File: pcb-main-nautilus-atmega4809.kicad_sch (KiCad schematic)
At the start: 0 parts

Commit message: Add power sheet
Supports #2.
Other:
- added sheet Power (pcb-main-nautilus-atmega4809-sheet-power.kicad_sch)
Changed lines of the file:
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@@
     (comment 1 "Derivative of the \"Arduino UNO Rev3\" (https://docs.arduino.cc/hardware/uno-rev3) and\\n\"Arduino Nano Every\" (https://docs.arduino.cc/hardware/nano-every) reference designs")
+  )
+  (sheet (at 69.85 66.04) (size 19.05 12.7) (fields_autoplaced)
+    (stroke (width 0.1524) (type solid) (color 0 0 0 0))
+    (fill (color 0 0 0 0.0000))
+    (property "Sheet name" "Power" (id 0) (at 69.85 65.3284 0)
+      (effects (font (size 1.27 1.27)) (justify left bottom))
+    )
+    (property "Sheet file" "pcb-main-nautilus-atmega4809-sheet-power.kicad_sch" (id 1) (at 69.85 79.3246 0)
+      (effects (font (size 1.27 1.27)) (justify left top))
+    )
+    (pin "5V" output (at 88.9 71.12 0)
+      (effects (font (size 1.27 1.27)) (justify right))
+    )
+    (pin "USB_VBUS" input (at 69.85 73.66 180)
+      (effects (font (size 1.27 1.27)) (justify left))
+    )
+    (pin "PWRIN" input (at 69.85 68.58 180)
+      (effects (font (size 1.27 1.27)) (justify left))
+    )
+    (pin "VIN" bidirectional (at 69.85 71.12 180)
+      (effects (font (size 1.27 1.27)) (justify left))
+    )
+    (pin "GND" input (at 69.85 76.2 180)
+      (effects (font (size 1.27 1.27)) (justify left))
+    )
+    (pin "3.3V" output (at 88.9 73.66 0)
+      (effects (font (size 1.27 1.27)) (justify right))
+    )
   )
   (sheet_instances
     (path "/" (page "1"))
+    (path "/5a33ba3c-72f7-420a-981d-98ac038c5559" (page "2"))
+  )
+  (symbol_instances
+    (path "/5a33ba3c-72f7-420a-981d-98ac038c5559/7408636a-a4a9-4362-ba4c-0a06147634bc"
+      (reference "C1") (unit 1) (value "47uF/25V") (footprint "")
+    )
+    (path "/5a33ba3c-72f7-420a-981d-98ac038c5559/b6fd6716-59a0-4f9a-985b-c7a8000096b3"
+      (reference "C2") (unit 1) (value "0.1uF/25V") (footprint "Capacitor_SMD:C_0603_1608Metric_Pad1.08x0.95mm_HandSolder")
+    )
+    (path "/5a33ba3c-72f7-420a-981d-98ac038c5559/982d25b7-d28f-455a-b867-22549e96b549"
+      (reference "C3") (unit 1) (value "47uF/6.3V") (footprint "")
+    )
+    (path "/5a33ba3c-72f7-420a-981d-98ac038c5559/d7420ce3-8bf9-42c3-93e9-9fdeab6607ed"
+      (reference "C4") (unit 1) (value "10uF/6.3V") (footprint "Capacitor_SMD:C_0603_1608Metric_Pad1.08x0.95mm_HandSolder")
+    )
+    (path "/5a33ba3c-72f7-420a-981d-98ac038c5559/a047b6c3-e0b4-4f5c-b490-a9c4fb048b22"
+      (reference "C5") (unit 1) (value "0.1uF/10V") (footprint "Capacitor_SMD:C_0603_1608Metric_Pad1.08x0.95mm_HandSolder")
+    )
+    (path "/5a33ba3c-72f7-420a-981d-98ac038c5559/5b44939b-18bc-4c09-9250-24b4ff8f8595"
+      (reference "C6") (unit 1) (value "0.1uF/10V") (footprint "Capacitor_SMD:C_0603_1608Metric_Pad1.08x0.95mm_HandSolder")
+    )
+    (path "/5a33ba3c-72f7-420a-981d-98ac038c5559/77a97430-fc8a-45b8-a5b5-ea674944d8bd"
+      (reference "D1") (unit 1) (value "20V/1A") (footprint "Diode_SMD:D_SOD-123F")
+    )
+    (path "/5a33ba3c-72f7-420a-981d-98ac038c5559/b95300ed-137f-43f2-ae28-165cdad19d45"
+      (reference "D2") (unit 1) (value "20V/1A") (footprint "Diode_SMD:D_SOD-123F")
+    )
+    (path "/5a33ba3c-72f7-420a-981d-98ac038c5559/29a8b156-103b-46fc-86a8-ec27533646aa"
+      (reference "D3") (unit 1) (value "GREEN") (footprint "LED_SMD:LED_0603_1608Metric_Pad1.05x0.95mm_HandSolder")
+    )
+    (path "/5a33ba3c-72f7-420a-981d-98ac038c5559/a21083b7-5749-4249-bcc1-55c3f0a221ff"
+      (reference "D4") (unit 1) (value "GREEN") (footprint "LED_SMD:LED_0603_1608Metric_Pad1.05x0.95mm_HandSolder")
+    )
+    (path "/5a33ba3c-72f7-420a-981d-98ac038c5559/3e98dc00-be45-4498-ad45-de614d277a00"
+      (reference "R1") (unit 1) (value "330/0.1W") (footprint "Resistor_SMD:R_0603_1608Metric_Pad0.98x0.95mm_HandSolder")
+    )
+    (path "/5a33ba3c-72f7-420a-981d-98ac038c5559/cf4e4292-169e-4011-8d76-bdce8a544dc4"
+      (reference "R2") (unit 1) (value "330/0.1W") (footprint "Resistor_SMD:R_0603_1608Metric_Pad0.98x0.95mm_HandSolder")
+    )
+    (path "/5a33ba3c-72f7-420a-981d-98ac038c5559/678f9d4d-d6a2-4e0c-8b54-d5be33abe55a"
+      (reference "U1") (unit 1) (value "NCP1117-5.0_TO252") (footprint "Package_TO_SOT_SMD:TO-252-2")
+    )
+    (path "/5a33ba3c-72f7-420a-981d-98ac038c5559/f9f27459-88f7-42f2-9098-bfb9e793b468"
+      (reference "U2") (unit 1) (value "AP2112K-3.3") (footprint "Package_TO_SOT_SMD:SOT-23-5")
+    )
   )
 )

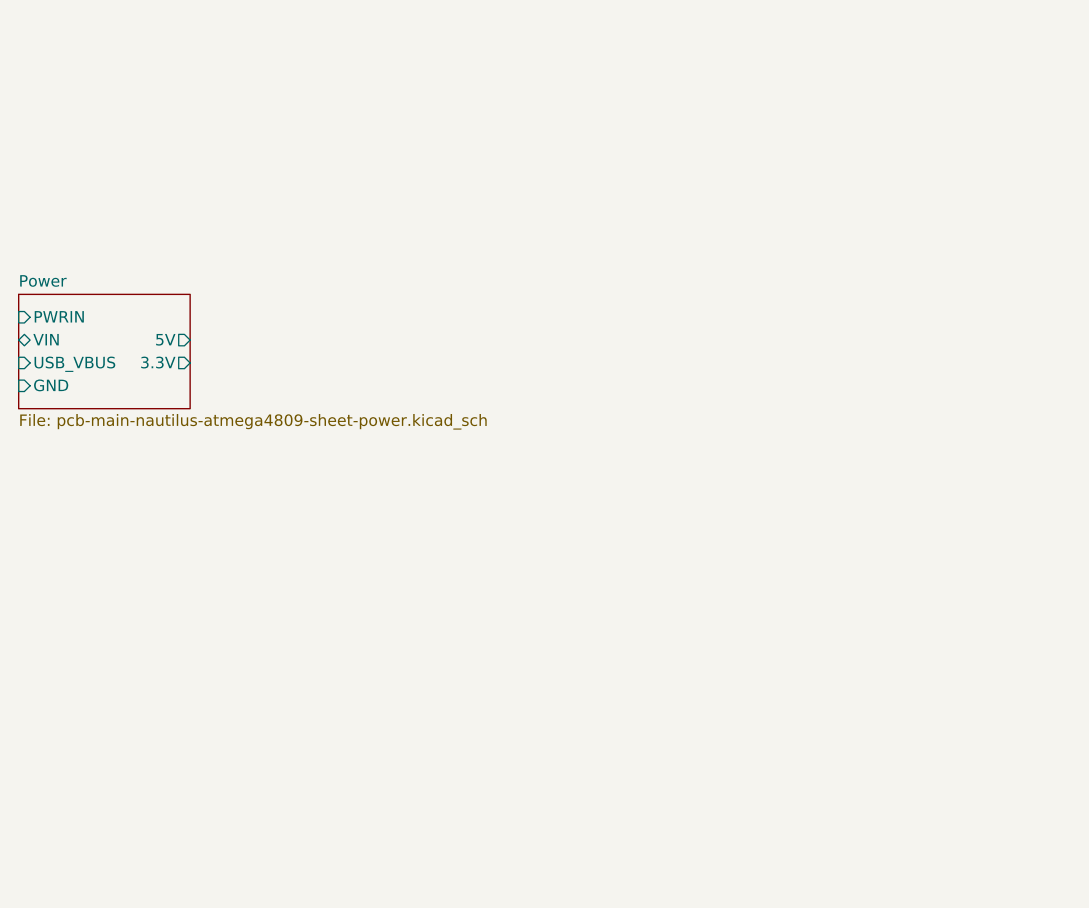
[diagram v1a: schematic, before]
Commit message: Add UPDI programmer and USB-serial bridge sheet
Supports #2.
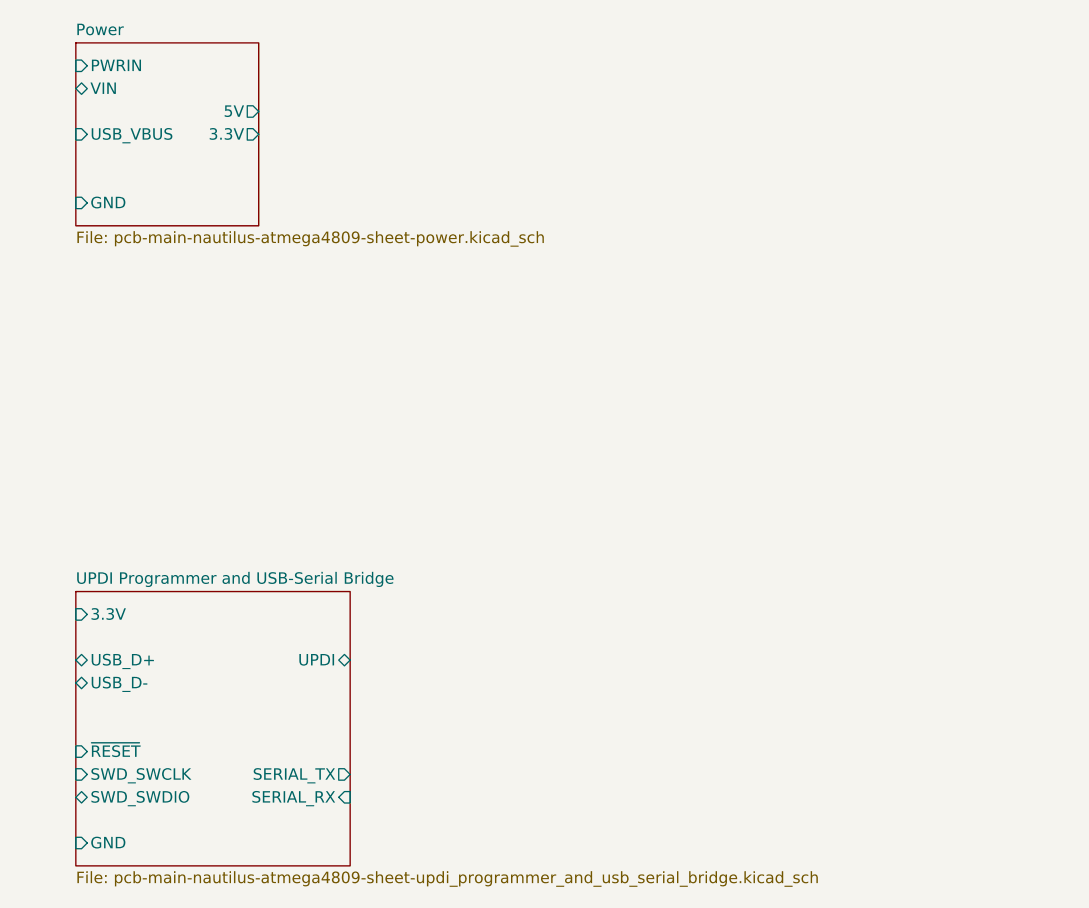
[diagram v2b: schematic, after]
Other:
- added sheet UPDI Programmer and USB-Serial Bridge (pcb-main-nautilus-atmega4809-sheet-updi_programmer_and_usb_serial_bridge.kicad_sch)
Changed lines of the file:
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@@
     (comment 1 "Derivative of the \"Arduino UNO Rev3\" (https://docs.arduino.cc/hardware/uno-rev3) and\\n\"Arduino Nano Every\" (https://docs.arduino.cc/hardware/nano-every) reference designs")
   )
-  (sheet (at 69.85 66.04) (size 19.05 12.7) (fields_autoplaced)
+  (sheet (at 76.2 38.1) (size 20.32 20.32) (fields_autoplaced)
     (stroke (width 0.1524) (type solid) (color 0 0 0 0))
     (fill (color 0 0 0 0.0000))
-    (property "Sheet name" "Power" (id 0) (at 69.85 65.3284 0)
+    (property "Sheet name" "Power" (id 0) (at 76.2 37.3884 0)
       (effects (font (size 1.27 1.27)) (justify left bottom))
     )
-    (property "Sheet file" "pcb-main-nautilus-atmega4809-sheet-power.kicad_sch" (id 1) (at 69.85 79.3246 0)
+    (property "Sheet file" "pcb-main-nautilus-atmega4809-sheet-power.kicad_sch" (id 1) (at 76.2 59.0046 0)
       (effects (font (size 1.27 1.27)) (justify left top))
     )
-    (pin "5V" output (at 88.9 71.12 0)
+    (pin "5V" output (at 96.52 45.72 0)
       (effects (font (size 1.27 1.27)) (justify right))
     )
-    (pin "USB_VBUS" input (at 69.85 73.66 180)
+    (pin "USB_VBUS" input (at 76.2 48.26 180)
       (effects (font (size 1.27 1.27)) (justify left))
     )
-    (pin "PWRIN" input (at 69.85 68.58 180)
+    (pin "PWRIN" input (at 76.2 40.64 180)
       (effects (font (size 1.27 1.27)) (justify left))
     )
-    (pin "VIN" bidirectional (at 69.85 71.12 180)
+    (pin "VIN" bidirectional (at 76.2 43.18 180)
       (effects (font (size 1.27 1.27)) (justify left))
     )
-    (pin "GND" input (at 69.85 76.2 180)
+    (pin "GND" input (at 76.2 55.88 180)
       (effects (font (size 1.27 1.27)) (justify left))
     )
-    (pin "3.3V" output (at 88.9 73.66 0)
+    (pin "3.3V" output (at 96.52 48.26 0)
+      (effects (font (size 1.27 1.27)) (justify right))
+    )
+  )
+  (sheet (at 76.2 99.06) (size 30.48 30.48) (fields_autoplaced)
+    (stroke (width 0.1524) (type solid) (color 0 0 0 0))
+    (fill (color 0 0 0 0.0000))
+    (property "Sheet name" "UPDI Programmer and USB-Serial Bridge" (id 0) (at 76.2 98.3484 0)
+      (effects (font (size 1.27 1.27)) (justify left bottom))
+    )
+    (property "Sheet file" "pcb-main-nautilus-atmega4809-sheet-updi_programmer_and_usb_serial_bridge.kicad_sch" (id 1) (at 76.2 130.1246 0)
+      (effects (font (size 1.27 1.27)) (justify left top))
+    )
+    (pin "SWD_SWCLK" input (at 76.2 119.38 180)
+      (effects (font (size 1.27 1.27)) (justify left))
+    )
+    (pin "SWD_SWDIO" bidirectional (at 76.2 121.92 180)
+      (effects (font (size 1.27 1.27)) (justify left))
+    )
+    (pin "GND" input (at 76.2 127 180)
+      (effects (font (size 1.27 1.27)) (justify left))
+    )
+    (pin "3.3V" input (at 76.2 101.6 180)
+      (effects (font (size 1.27 1.27)) (justify left))
+    )
+    (pin "~{RESET}" input (at 76.2 116.84 180)
+      (effects (font (size 1.27 1.27)) (justify left))
+    )
+    (pin "USB_D+" bidirectional (at 76.2 106.68 180)
+      (effects (font (size 1.27 1.27)) (justify left))
+    )
+    (pin "USB_D-" bidirectional (at 76.2 109.22 180)
+      (effects (font (size 1.27 1.27)) (justify left))
+    )
+    (pin "SERIAL_RX" input (at 106.68 121.92 0)
+      (effects (font (size 1.27 1.27)) (justify right))
+    )
+    (pin "SERIAL_TX" output (at 106.68 119.38 0)
+      (effects (font (size 1.27 1.27)) (justify right))
+    )
+    (pin "UPDI" bidirectional (at 106.68 106.68 0)
       (effects (font (size 1.27 1.27)) (justify right))
     )
@@
     (path "/" (page "1"))
     (path "/5a33ba3c-72f7-420a-981d-98ac038c5559" (page "2"))
+    (path "/9563730f-8d1a-4fdb-af84-834004e725da" (page "3"))
   )
   (symbol_instances
@@
     )
     (path "/5a33ba3c-72f7-420a-981d-98ac038c5559/982d25b7-d28f-455a-b867-22549e96b549"
-      (reference "C3") (unit 1) (value "47uF/6.3V") (footprint "")
+      (reference "C3") (unit 1) (value "47uF/10V") (footprint "")
+    )
+    (path "/5a33ba3c-72f7-420a-981d-98ac038c5559/a047b6c3-e0b4-4f5c-b490-a9c4fb048b22"
+      (reference "C4") (unit 1) (value "0.1uF/10V") (footprint "Capacitor_SMD:C_0603_1608Metric_Pad1.08x0.95mm_HandSolder")
     )
     (path "/5a33ba3c-72f7-420a-981d-98ac038c5559/d7420ce3-8bf9-42c3-93e9-9fdeab6607ed"
-      (reference "C4") (unit 1) (value "10uF/6.3V") (footprint "Capacitor_SMD:C_0603_1608Metric_Pad1.08x0.95mm_HandSolder")
-    )
-    (path "/5a33ba3c-72f7-420a-981d-98ac038c5559/a047b6c3-e0b4-4f5c-b490-a9c4fb048b22"
-      (reference "C5") (unit 1) (value "0.1uF/10V") (footprint "Capacitor_SMD:C_0603_1608Metric_Pad1.08x0.95mm_HandSolder")
+      (reference "C5") (unit 1) (value "10uF/6.3V") (footprint "Capacitor_SMD:C_0603_1608Metric_Pad1.08x0.95mm_HandSolder")
     )
     (path "/5a33ba3c-72f7-420a-981d-98ac038c5559/5b44939b-18bc-4c09-9250-24b4ff8f8595"
       (reference "C6") (unit 1) (value "0.1uF/10V") (footprint "Capacitor_SMD:C_0603_1608Metric_Pad1.08x0.95mm_HandSolder")
+    )
+    (path "/9563730f-8d1a-4fdb-af84-834004e725da/d2d9feeb-a0ae-4ffe-80a8-16fa1ddcf5b8"
+      (reference "C7") (unit 1) (value "4.7uF/10V") (footprint "Capacitor_SMD:C_0603_1608Metric_Pad1.08x0.95mm_HandSolder")
+    )
+    (path "/9563730f-8d1a-4fdb-af84-834004e725da/75fddebe-6b60-4818-a476-4ffe9d32d1f5"
+      (reference "C8") (unit 1) (value "0.1uF/10V") (footprint "Capacitor_SMD:C_0603_1608Metric_Pad1.08x0.95mm_HandSolder")
+    )
+    (path "/9563730f-8d1a-4fdb-af84-834004e725da/0ab0dcb0-de7e-4820-b2c9-59f15c46f76b"
+      (reference "C9") (unit 1) (value "0.1uF/10V") (footprint "Capacitor_SMD:C_0603_1608Metric_Pad1.08x0.95mm_HandSolder")
     )
     (path "/5a33ba3c-72f7-420a-981d-98ac038c5559/77a97430-fc8a-45b8-a5b5-ea674944d8bd"
@@
       (reference "D4") (unit 1) (value "GREEN") (footprint "LED_SMD:LED_0603_1608Metric_Pad1.05x0.95mm_HandSolder")
     )
+    (path "/9563730f-8d1a-4fdb-af84-834004e725da/e8c125a0-c891-462e-9bd4-251e59b83fd3"
+      (reference "NT1") (unit 1) (value "NetTie_3") (footprint "")
+    )
     (path "/5a33ba3c-72f7-420a-981d-98ac038c5559/3e98dc00-be45-4498-ad45-de614d277a00"
       (reference "R1") (unit 1) (value "330/0.1W") (footprint "Resistor_SMD:R_0603_1608Metric_Pad0.98x0.95mm_HandSolder")
@@
     (path "/5a33ba3c-72f7-420a-981d-98ac038c5559/cf4e4292-169e-4011-8d76-bdce8a544dc4"
       (reference "R2") (unit 1) (value "330/0.1W") (footprint "Resistor_SMD:R_0603_1608Metric_Pad0.98x0.95mm_HandSolder")
+    )
+    (path "/9563730f-8d1a-4fdb-af84-834004e725da/90972ee7-7e53-4f95-af2f-bd6dbb00fdf9"
+      (reference "R3") (unit 1) (value "4.7k/0.1W") (footprint "Resistor_SMD:R_0603_1608Metric_Pad0.98x0.95mm_HandSolder")
+    )
+    (path "/9563730f-8d1a-4fdb-af84-834004e725da/f1e4345f-c080-4ad6-9675-48866056f5d2"
+      (reference "R4") (unit 1) (value "4.7k/0.1W") (footprint "Resistor_SMD:R_0603_1608Metric_Pad0.98x0.95mm_HandSolder")
     )
     (path "/5a33ba3c-72f7-420a-981d-98ac038c5559/678f9d4d-d6a2-4e0c-8b54-d5be33abe55a"
@@
       (reference "U2") (unit 1) (value "AP2112K-3.3") (footprint "Package_TO_SOT_SMD:SOT-23-5")
     )
+    (path "/9563730f-8d1a-4fdb-af84-834004e725da/7bdba785-3a36-4aa4-a9a0-021b0af85017"
+      (reference "U3") (unit 1) (value "ATSAMD11D14A-SS") (footprint "Package_SO:SOIC-20W_7.5x12.8mm_P1.27mm")
+    )
   )
